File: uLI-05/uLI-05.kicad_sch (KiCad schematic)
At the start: 0 parts

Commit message: Copy schematics from uLI-04.
Changes compared to uLI-04:
* Add SM712 protection to Ale asiXpressNET
* Add ESDA6V1 protection to USB
* Change prog connector pnout to match PICKit
* Unify pull-ups to 10k
* Connect ADM2483's PV directly to VCC
* Use 78M05 instead of 78L05
* Use 22R resistor just to connect capacitor
* Add 10k pull-down to PGM
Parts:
- added C1, C4, C5, C6, C7: 100n, symbol Device:C
- added C2, C3: 22p, symbol Device:C
- added C8: 22u/25V, symbol Device:C
- added C9: 470n, symbol Device:C
- added D1: SM712_SOT23, Package_TO_SOT_SMD:SOT-23, symbol Diode:SM712_SOT23
- added D2: ESDA6V1-5SC6, Package_TO_SOT_SMD:SOT-23-6, symbol Power_Protection:ESDA6V1-5SC6
- added D3: D_Schottky, symbol Device:D_Schottky
- added D4: RED, symbol Device:LED
- added D5: D, symbol Device:D_Schottky
- added D6: BLUE, symbol Device:LED
- added D7, D8: GREEN, symbol Device:LED
- added D9: YELLOW, symbol Device:LED
- added J1, J2: RJ25, symbol Connector:RJ25
- added J3: USB_B, symbol Connector:USB_B
- added J4: C, symbol Connector_Generic:Conn_01x02
- added J5: PROG, symbol Connector_Generic:Conn_01x06
- added JP1: Jumper_2_Open, symbol Jumper:Jumper_2_Open
- added Q1: IRF7306, Package_SO:SOIC-8_3.9x4.9mm_P1.27mm, symbol Transistor_FET:IRF7324
- added R1, R2: 100k, symbol Device:R
- added R10, R3, R4, R6: 10k, symbol Device:R
- added R11, R12, R13, R5, R8, R9: 2k2, symbol Device:R
- added R14: 1k, symbol Device:R
- added R7: 22R, symbol Device:R
- added U1: ADM2483xRW, Package_SO:SOIC-16W_7.5x10.3mm_P1.27mm, symbol Interface_UART:ADM2483xRW
- added U2: LM78M05_TO252, Package_TO_SOT_SMD:TO-252-2, symbol Regulator_Linear:LM78M05_TO252
- added U3, U4: PC817, Package_DIP:DIP-4_W7.62mm, symbol Isolator:PC817
- added U5: PIC18F14K50-EP, Package_DIP:DIP-20_W7.62mm, symbol MCU_Microchip_PIC18:PIC18F14K50-EP
- added Y1: 12MHz, symbol Device:Crystal
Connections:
- new net: D4.2 (A), R5.2
- new net: D7.2 (A), R11.2
- new net: C2.1, U5.3 (RA4/IOCA3/AN3/OSC2/CLKOUT), Y1.1
- new net: C3.2, U5.2 (RA5/IOCA5/OSC1/CLKIN), Y1.2
- new net: J5.2 (Pin_2), JP1.2 (B)
- new net: D8.2 (A), R12.2
- new net: D6.2 (A), R8.2
- new net: J1.5, J2.5, Q1.5 (D2), Q1.6 (D2), Q1.7 (D1), Q1.8 (D1), R5.1
- new net: D3.2 (A), J4.1 (Pin_1)
- new net: D9.2 (A), R13.2
- new net: R9.1, U4.1
- new net: C8.1, D5.2 (A), R7.2
- new net: R14.2, U5.6 (SRQ/C12OUT/P1B/RC4)
- new net: C9.1, U5.17 (VUSB)
- new net +12VA: C7.1, D3.1 (K), D5.1 (K), Q1.1 (S1), Q1.3 (S2), R6.1, R7.1, R8.1, R9.2, U2.1 (VI)
- new net +5VA: C5.1, C6.1, R1.1, U1.16 (VDD2), U2.3 (VO)
- new net A: D1.1 (A1), J1.4, J2.4, R1.2, U1.12 (A)
- new net B: D1.2 (A2), J1.3, J2.3, R2.1, U1.13 (B)
- new net D+/PGD: D2.1 (IO1), D2.6 (IO5), J3.3 (D+), J5.4 (Pin_4), U5.19 (RA0/IOCA0/D+/PGD)
- new net D-/PGC: D2.4 (IO3), D2.5 (IO4), J3.2 (D-), J5.5 (Pin_5), U5.18 (RA1/IOCA1/D-/PGC)
- new net DE: U1.4 (~{RE}), U1.5 (DE), U5.11 (RB6/IOCB6/SCK/SCL)
- new net GND: C1.2, C2.2, C3.1, C4.2, C9.2, D2.2 (GND), J3.4 (GND), J5.3 (Pin_3), R3.2, U1.2 (GND1), U1.8 (GND1), U3.2, U4.3, U5.20 (VSS)
- new net GNDA: C5.2, C6.2, C7.2, C8.2, D1.3 (common), D4.1 (K), D6.1 (K), D7.1 (K), D8.1 (K), D9.1 (K), J1.2, J2.2, J4.2 (Pin_2), R2.2, U1.15 (GND2), U1.9 (GND2), U2.2 (GND), U3.3, U4.2
- new net LED_GR1: R11.1, U5.15 (INT1/C12IN1-/VREF-AN5/RC1)
- new net LED_GR2: R12.1, U5.16 (INT0/C12IN+/VREF+/AN4/RC0)
- new net LED_YEL: R13.1, U5.14 (INT2/CVREF/C12IN2-/P1D/AN6/RC2)
- new net MCLR: J5.1 (Pin_1), R4.2, U5.4 (RA3/IOCA3/~{MCLR}/Vpp)
- new net PGM: J5.6 (Pin_6), R3.1, U5.7 (PGM/C12IN3-/P1C/AN7/RC3)
- new net POWER: R14.1, U3.1
- new net POWERA: Q1.2 (G1), Q1.4 (G2), R6.2, U3.4
- new net RX: U1.3 (RxD), U5.12 (RB5/IOCB5/AN11/RX/DT)
- new net SENSE: R10.2, U4.4, U5.13 (RB4/IOCB4/AN10/SDI/SDA)
- new net TX: U1.6 (TxD), U5.10 (RB7/IOCB7/TX/CK)
- new net VCC: C1.1, C4.1, J3.1 (VBUS), JP1.1 (A), R10.1, R4.1, U1.1 (VDD1), U1.7 (PV), U5.1 (VDD)
- no-connect marks 0 -> 8

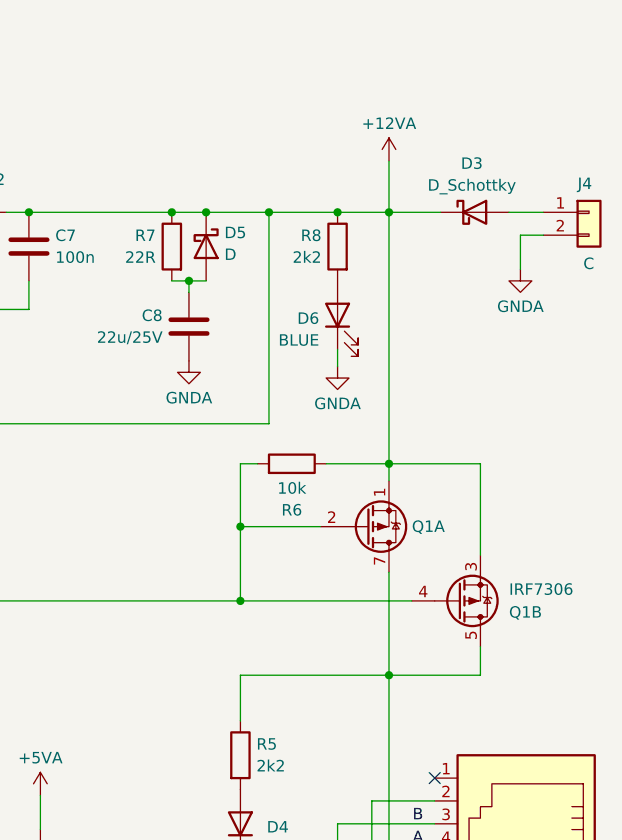
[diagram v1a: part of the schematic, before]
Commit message: Add another diode to power supply.
So XpressNET devices do not drain our internal capacitors.
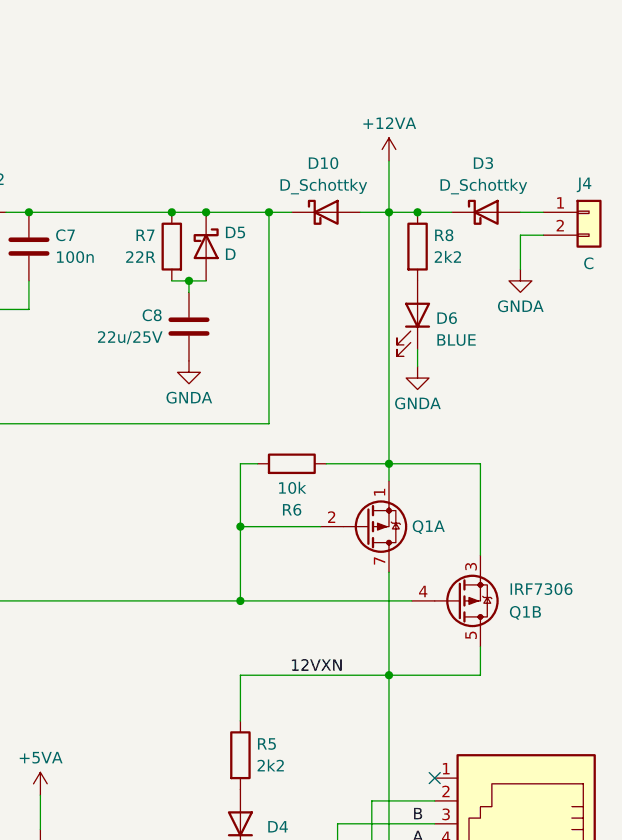
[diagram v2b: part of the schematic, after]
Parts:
- added D10: D_Schottky, symbol Device:D_Schottky
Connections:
- net +12VA: now also D10.2 (A); no longer C7.1, D5.1 (K), R7.1, R9.2, U2.1 (VI)
- net 12VXN: now reaches J1.5, J2.5, Q1.5 (D2), Q1.6 (D2), Q1.7 (D1), Q1.8 (D1), R5.1
- new net: C7.1, D10.1 (K), D5.1 (K), R7.1, R9.2, U2.1 (VI)
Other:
- title: uLI 05 -> uLI-05
- moved on the sheet: D3, D6, R8
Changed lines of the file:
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@@
   (paper "A4")
   (title_block
-    (title "uLI 05")
+    (title "uLI-05")
     (date "2024-02-15")
     (rev "5.0")
@@
   (junction (at 256.54 125.73) (diameter 0) (color 0 0 0 0)
   )
+  (junction (at 261.62 35.56) (diameter 0) (color 0 0 0 0)
+  )
   (junction (at 104.775 59.055) (diameter 0) (color 0 0 0 0)
   )
@@
   )
   (junction (at 248.285 120.015) (diameter 0) (color 0 0 0 0)
-  )
-  (junction (at 252.73 35.56) (diameter 0) (color 0 0 0 0)
   )
   (junction (at 258.445 108.585) (diameter 0) (color 0 0 0 0)
@@
     (stroke (width 0) (type default))
   )
+  (wire (pts (xy 261.62 35.56) (xy 265.43 35.56))
+    (stroke (width 0) (type default))
+  )
   (wire (pts (xy 175.26 56.515) (xy 175.26 59.055))
     (stroke (width 0) (type default))
@@
     (stroke (width 0) (type default))
   )
-  (wire (pts (xy 252.73 35.56) (xy 258.445 35.56))
-    (stroke (width 0) (type default))
-  )
   (wire (pts (xy 219.71 130.81) (xy 219.71 139.7))
     (stroke (width 0) (type default))
@@
   )
   (wire (pts (xy 104.775 59.055) (xy 104.775 69.215))
-    (stroke (width 0) (type default))
-  )
-  (wire (pts (xy 258.445 35.56) (xy 264.16 35.56))
     (stroke (width 0) (type default))
   )
@@
     (stroke (width 0) (type default))
   )
-  (wire (pts (xy 271.78 35.56) (xy 275.59 35.56))
+  (wire (pts (xy 273.05 35.56) (xy 275.59 35.56))
     (stroke (width 0) (type default))
   )
@@
     (stroke (width 0) (type default))
   )
+  (wire (pts (xy 255.27 35.56) (xy 258.445 35.56))
+    (stroke (width 0) (type default))
+  )
   (wire (pts (xy 194.31 83.82) (xy 198.12 83.82))
     (stroke (width 0) (type default))
@@
     (stroke (width 0) (type default))
   )
+  (wire (pts (xy 258.445 35.56) (xy 261.62 35.56))
+    (stroke (width 0) (type default))
+  )
   (wire (pts (xy 35.56 109.855) (xy 35.56 111.76))
     (stroke (width 0) (type default))
@@
     (stroke (width 0) (type default))
   )
+  (wire (pts (xy 245.11 35.56) (xy 247.65 35.56))
+    (stroke (width 0) (type default))
+  )
   (wire (pts (xy 205.105 59.055) (xy 245.11 59.055))
     (stroke (width 0) (type default))
@@
     (stroke (width 0) (type default))
   )
-  (wire (pts (xy 245.11 35.56) (xy 252.73 35.56))
-    (stroke (width 0) (type default))
-  )
   (wire (pts (xy 167.005 122.555) (xy 167.005 114.935))
     (stroke (width 0) (type default))
@@
     (stroke (width 0) (type default))
   )
-  (wire (pts (xy 252.73 52.705) (xy 252.73 50.8))
+  (wire (pts (xy 261.62 52.705) (xy 261.62 50.8))
     (stroke (width 0) (type default))
   )
@@
   )
   (label "D+{slash}PGD" (at 65.405 76.835 180) (fields_autoplaced)
+    (effects (font (size 1.27 1.27)) (justify right bottom))
+  )
+  (label "12VXN" (at 253.365 86.995 180) (fields_autoplaced)
     (effects (font (size 1.27 1.27)) (justify right bottom))
   )
@@
         (path "/78ef7769-d6f1-48f5-a16b-8d45b14bfe28"
           (reference "#PWR039") (unit 1)
+        )
+      )
+    )
+  )
+  (symbol (lib_id "Device:D_Schottky") (at 251.46 35.56 0) (unit 1)
+    (in_bom yes) (on_board yes) (dnp no) (fields_autoplaced)
+    (property "Reference" "D10" (at 251.1425 30.1457 0)
+      (effects (font (size 1.27 1.27)))
+    )
+    (property "Value" "D_Schottky" (at 251.1425 32.5699 0)
+      (effects (font (size 1.27 1.27)))
+    )
+    (property "Footprint" "" (at 251.46 35.56 0)
+      (effects (font (size 1.27 1.27)) hide)
+    )
+    (property "Datasheet" "~" (at 251.46 35.56 0)
+      (effects (font (size 1.27 1.27)) hide)
+    )
+    (pin "1")
+    (pin "2")
+    (instances
+      (project "uLI-05"
+        (path "/78ef7769-d6f1-48f5-a16b-8d45b14bfe28"
+          (reference "D10") (unit 1)
         )
       )
@@
     )
   )
-  (symbol (lib_id "Device:LED") (at 252.73 46.99 90) (unit 1)
+  (symbol (lib_id "Device:LED") (at 261.62 46.99 270) (mirror x) (unit 1)
     (in_bom yes) (on_board yes) (dnp no)
-    (property "Reference" "D6" (at 250.698 47.3654 90)
-      (effects (font (size 1.27 1.27)) (justify left))
-    )
-    (property "Value" "BLUE" (at 250.698 49.7896 90)
-      (effects (font (size 1.27 1.27)) (justify left))
-    )
-    (property "Footprint" "" (at 252.73 46.99 0)
-      (effects (font (size 1.27 1.27)) hide)
-    )
-    (property "Datasheet" "~" (at 252.73 46.99 0)
+    (property "Reference" "D6" (at 263.652 47.3654 90)
+      (effects (font (size 1.27 1.27)) (justify left))
+    )
+    (property "Value" "BLUE" (at 263.652 49.7896 90)
+      (effects (font (size 1.27 1.27)) (justify left))
+    )
+    (property "Footprint" "" (at 261.62 46.99 0)
+      (effects (font (size 1.27 1.27)) hide)
+    )
+    (property "Datasheet" "~" (at 261.62 46.99 0)
       (effects (font (size 1.27 1.27)) hide)
     )
@@
     )
   )
-  (symbol (lib_id "power:GNDA") (at 252.73 52.705 0) (mirror y) (unit 1)
-    (in_bom yes) (on_board yes) (dnp no) (fields_autoplaced)
-    (property "Reference" "#PWR031" (at 252.73 59.055 0)
-      (effects (font (size 1.27 1.27)) hide)
-    )
-    (property "Value" "GNDA" (at 252.73 56.8381 0)
-      (effects (font (size 1.27 1.27)))
-    )
-    (property "Footprint" "" (at 252.73 52.705 0)
-      (effects (font (size 1.27 1.27)) hide)
-    )
-    (property "Datasheet" "" (at 252.73 52.705 0)
+  (symbol (lib_id "power:GNDA") (at 261.62 52.705 0) (unit 1)
+    (in_bom yes) (on_board yes) (dnp no) (fields_autoplaced)
+    (property "Reference" "#PWR031" (at 261.62 59.055 0)
+      (effects (font (size 1.27 1.27)) hide)
+    )
+    (property "Value" "GNDA" (at 261.62 56.8381 0)
+      (effects (font (size 1.27 1.27)))
+    )
+    (property "Footprint" "" (at 261.62 52.705 0)
+      (effects (font (size 1.27 1.27)) hide)
+    )
+    (property "Datasheet" "" (at 261.62 52.705 0)
       (effects (font (size 1.27 1.27)) hide)
     )
@@
     )
   )
-  (symbol (lib_id "Device:D_Schottky") (at 267.97 35.56 0) (unit 1)
-    (in_bom yes) (on_board yes) (dnp no) (fields_autoplaced)
-    (property "Reference" "D3" (at 267.6525 30.1457 0)
-      (effects (font (size 1.27 1.27)))
-    )
-    (property "Value" "D_Schottky" (at 267.6525 32.5699 0)
-      (effects (font (size 1.27 1.27)))
-    )
-    (property "Footprint" "" (at 267.97 35.56 0)
-      (effects (font (size 1.27 1.27)) hide)
-    )
-    (property "Datasheet" "~" (at 267.97 35.56 0)
+  (symbol (lib_id "Device:D_Schottky") (at 269.24 35.56 0) (unit 1)
+    (in_bom yes) (on_board yes) (dnp no) (fields_autoplaced)
+    (property "Reference" "D3" (at 268.9225 30.1457 0)
+      (effects (font (size 1.27 1.27)))
+    )
+    (property "Value" "D_Schottky" (at 268.9225 32.5699 0)
+      (effects (font (size 1.27 1.27)))
+    )
+    (property "Footprint" "" (at 269.24 35.56 0)
+      (effects (font (size 1.27 1.27)) hide)
+    )
+    (property "Datasheet" "~" (at 269.24 35.56 0)
       (effects (font (size 1.27 1.27)) hide)
     )
@@
     )
   )
-  (symbol (lib_id "Device:R") (at 252.73 39.37 0) (mirror y) (unit 1)
-    (in_bom yes) (on_board yes) (dnp no) (fields_autoplaced)
-    (property "Reference" "R8" (at 250.952 38.1579 0)
-      (effects (font (size 1.27 1.27)) (justify left))
-    )
-    (property "Value" "2k2" (at 250.952 40.5821 0)
-      (effects (font (size 1.27 1.27)) (justify left))
-    )
-    (property "Footprint" "" (at 254.508 39.37 90)
-      (effects (font (size 1.27 1.27)) hide)
-    )
-    (property "Datasheet" "~" (at 252.73 39.37 0)
-      (effects (font (size 1.27 1.27)) hide)
-    )
+  (symbol (lib_id "Device:R") (at 261.62 39.37 0) (unit 1)
+    (in_bom yes) (on_board yes) (dnp no) (fields_autoplaced)
+    (property "Reference" "R8" (at 263.398 38.1579 0)
+      (effects (font (size 1.27 1.27)) (justify left))
+    )
+    (property "Value" "2k2" (at 263.398 40.5821 0)
+      (effects (font (size 1.27 1.27)) (justify left))
+    )
+    (property "Footprint" "" (at 259.842 39.37 90)
+      (effects (font (size 1.27 1.27)) hide)
+    )
+    (property "Datasheet" "~" (at 261.62 39.37 0)
+      (effects (font (size 1.27 1.27)) hide)
+    )

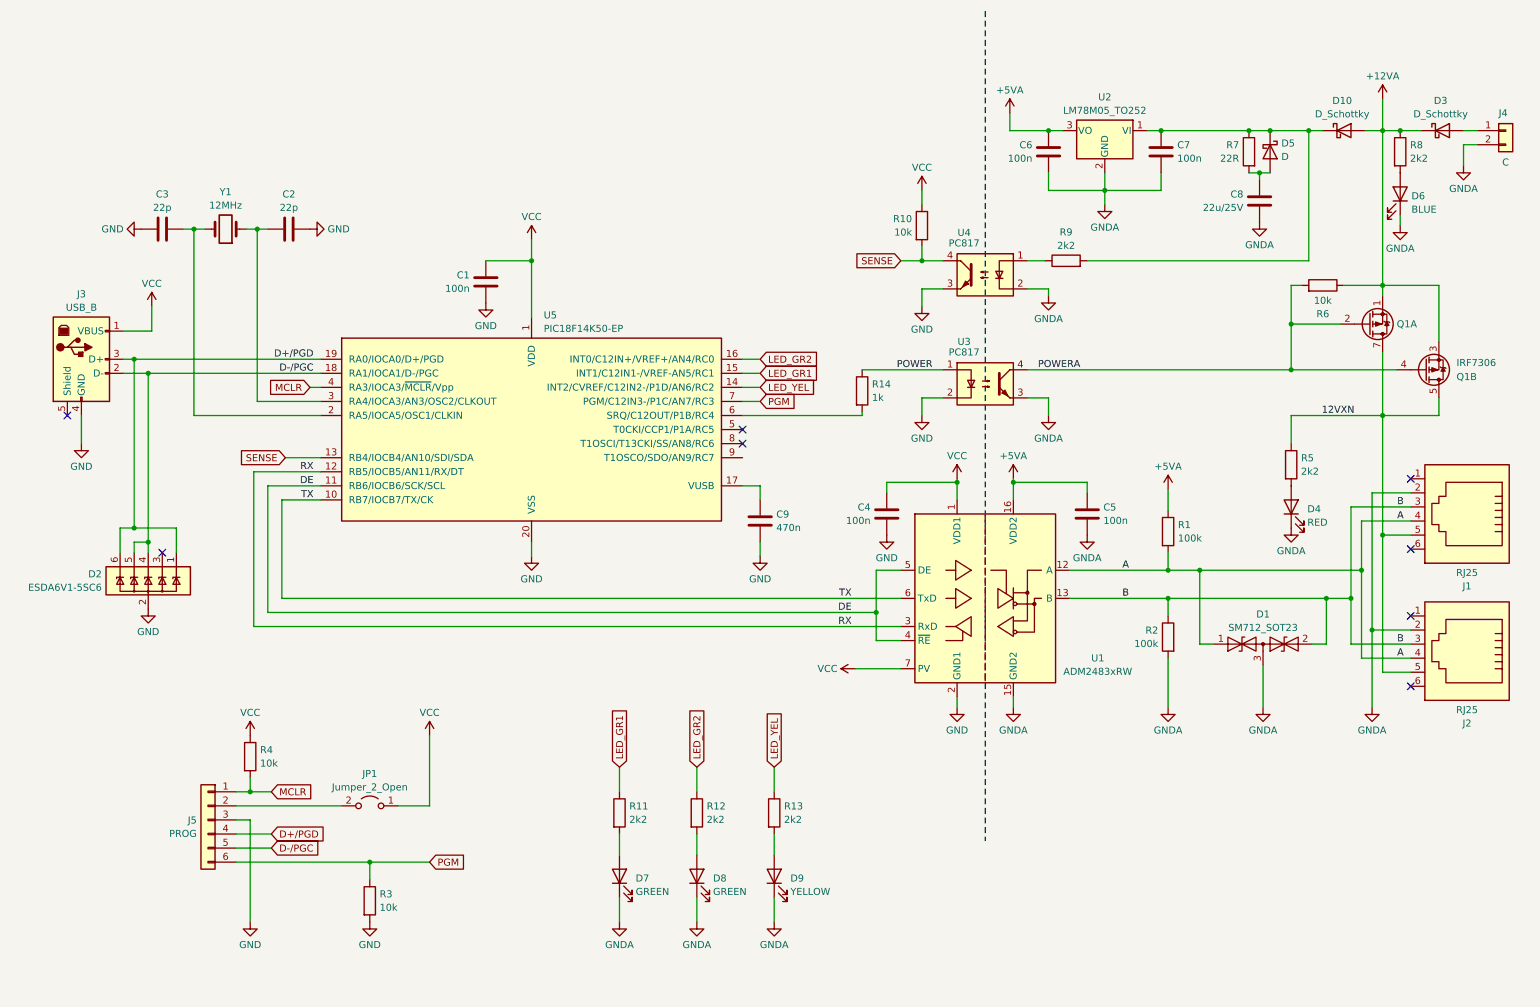
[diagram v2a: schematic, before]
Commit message: Add mounting holes, use 1N5819 as schottky diodes.
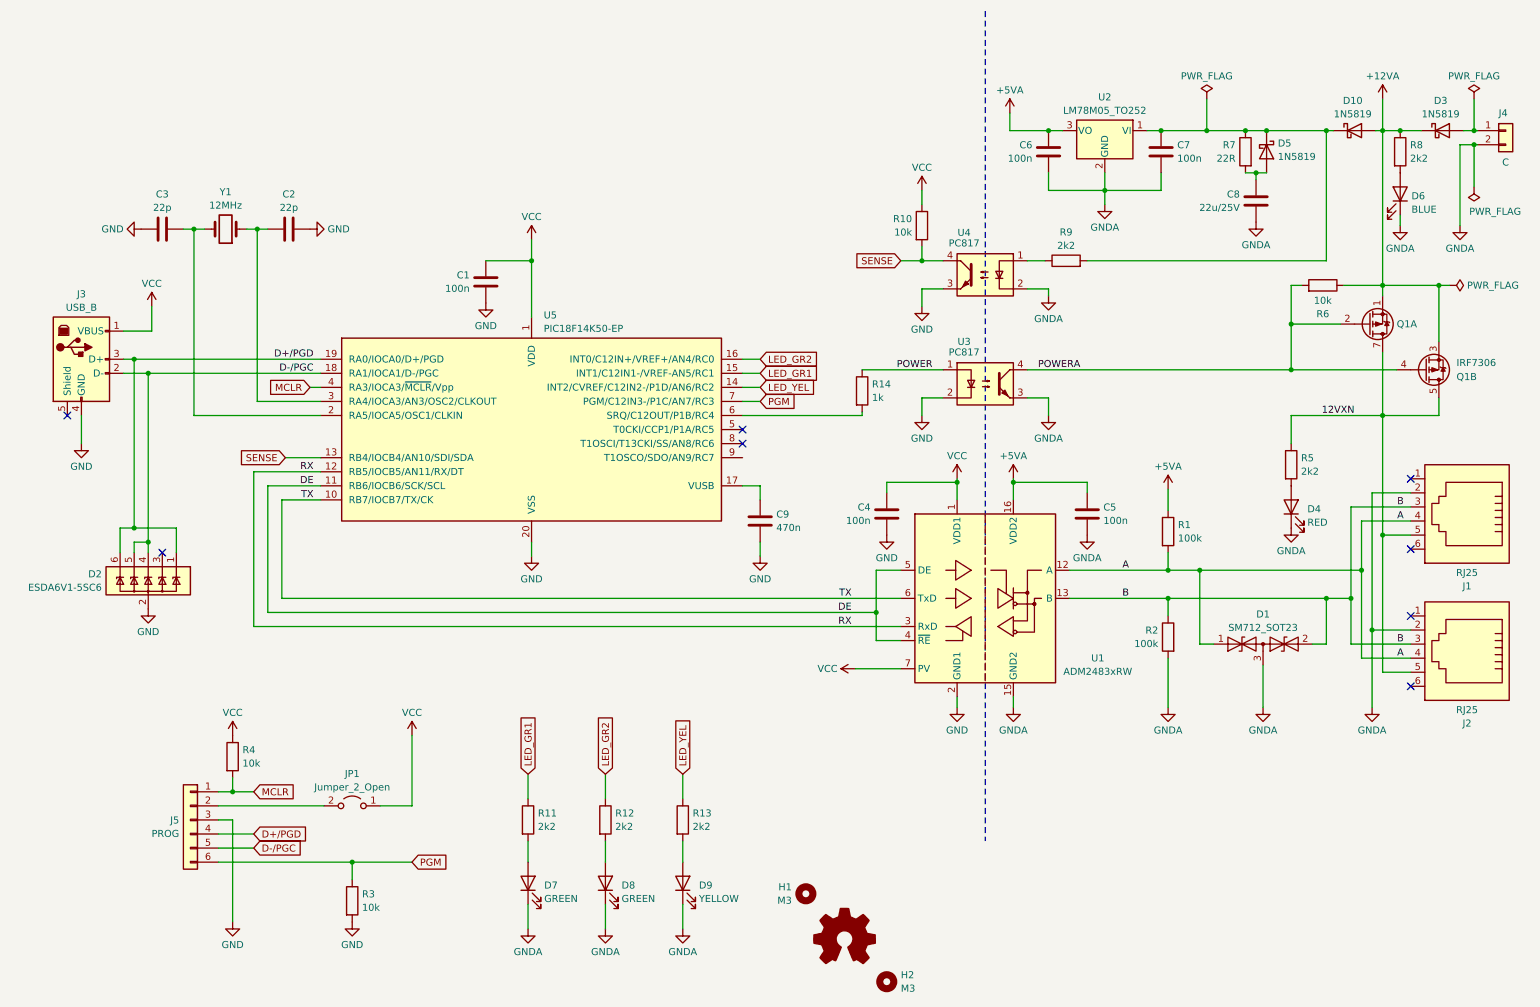
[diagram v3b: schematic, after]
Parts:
- added H1, H2: M3, symbol Mechanical:MountingHole
- D10, D3: value D_Schottky -> 1N5819
- D5: value D -> 1N5819
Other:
- moved on the sheet: C8, D10, D5, D7, D8, D9, J5, JP1, R11, R12, R13, R3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
